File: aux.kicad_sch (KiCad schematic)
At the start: 4 parts

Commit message: Schematic complete, maybe
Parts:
- removed U?: ADuM5211, Package_SO:SSOP-20_5.3x7.2mm_P0.65mm, symbol Isolator:ADuM5211
- added C853: 10u, Capacitor_SMD:C_0603_1608Metric, symbol Device:C
- added D85: BZX84C5V6, Package_TO_SOT_SMD:SOT-23, symbol Parts:BZX84Cxx
- added J85: USB_C_Receptacle_USB2.0_16P, symbol Connector:USB_C_Receptacle_USB2.0_16P
- added J86: Conn_01x02_Pin, symbol Connector:Conn_01x02_Pin
- added L86: 100, Inductor_SMD:L_0603_1608Metric, symbol Parts:L_Ferrite_Power
- added Q81: Si2301CDS, Package_TO_SOT_SMD:SOT-23, symbol External:Si2301CDS
- added Q82: AO3400A, Package_TO_SOT_SMD:SOT-23, symbol Transistor_FET:AO3400A
- added R563, R564: 100k, symbol Device:R
- added R851, R852: 5k1, symbol Device:R
- C851, C852: renamed from C?; LCSC (none) -> C307331
- U85: renamed from U?; footprint RTE0016D -> Package_DFN_QFN:Texas_RTE0016D_WQFN-16-1EP_3x3mm_P0.5mm_EP0.8x0.8mm; LCSC (none) -> C2863226
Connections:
- net GNDPWR: now also C853.2, D85.1 (A), J85.A1 (GND), J85.A12 (GND), J85.B1 (GND), J85.B12 (GND), J85.S1 (SHIELD), Q82.2 (S), R564.1, R851.2, R852.2
- new net: Q81.1 (G), Q82.3 (D), R563.2
- new net: J85.A5 (CC1), R851.1
- new net: J85.B5 (CC2), R852.1
- new net: J85.A4 (VBUS), J85.A9 (VBUS), J85.B4 (VBUS), J85.B9 (VBUS), L86.1
- new net +5V: C853.1, J86.2 (Pin_2), Q81.3 (D)
- new net +5VP: D85.3 (K), J86.1 (Pin_1), L86.2, Q81.2 (S), R563.1
- new net PWR_EN: Q82.1 (G), R564.2
- new net USB_D+: J85.A6 (D+), J85.B6 (D+)
- new net USB_D-: J85.A7 (D-), J85.B7 (D-)
- no-connect marks 1 -> 3
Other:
- moved on the sheet: C851, C852, U85

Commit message: Part selection
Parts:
- J85, J86: now left out of the parts list
- Q81: LCSC (none) -> C10487
- Q82: LCSC (none) -> C20917
- R563, R564: footprint (none) -> Resistor_SMD:R_0402_1005Metric; LCSC (none) -> C25741
- R851, R852: footprint (none) -> Resistor_SMD:R_0402_1005Metric; LCSC (none) -> C25905
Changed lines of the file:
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@@
+			)
+		)
+		(property "LCSC" "C10487"
+			(at 129.54 29.21 90)
+			(effects
+				(font
+					(size 1.27 1.27)
+				)
+				(hide yes)
 			)
 		)
@@
 			)
 		)
-		(property "Footprint" ""
+		(property "Footprint" "Resistor_SMD:R_0402_1005Metric"
 			(at 100.33 33.528 90)
 			(effects
@@
 			)
 		)
+		(property "LCSC" "C25905"
+			(at 100.33 31.75 90)
+			(effects
+				(font
+					(size 1.27 1.27)
+				)
+				(hide yes)
+			)
+		)
 		(pin "1"
 		)
@@
 			)
 		)
-		(property "Footprint" ""
+		(property "Footprint" "Resistor_SMD:R_0402_1005Metric"
 			(at 124.46 34.798 90)
 			(effects
@@
 		(property "Description" "Resistor"
 			(at 124.46 33.02 0)
+			(effects
+				(font
+					(size 1.27 1.27)
+				)
+				(hide yes)
+			)
+		)
+		(property "LCSC" "C25741"
+			(at 124.46 33.02 90)
 			(effects
 				(font
@@
 			)
 		)
-		(property "Footprint" ""
+		(property "Footprint" "Resistor_SMD:R_0402_1005Metric"
 			(at 100.33 32.512 90)
 			(effects
@@
 			)
 		)
+		(property "LCSC" "C25905"
+			(at 100.33 34.29 90)
+			(effects
+				(font
+					(size 1.27 1.27)
+				)
+				(hide yes)
+			)
+		)
 		(pin "1"
 		)
@@
 		(unit 1)
 		(exclude_from_sim no)
-		(in_bom yes)
+		(in_bom no)
 		(on_board yes)
 		(dnp no)
@@
 		(unit 1)
 		(exclude_from_sim no)
-		(in_bom yes)
+		(in_bom no)
 		(on_board yes)
 		(dnp no)
@@
 			)
 		)
+		(property "LCSC" "C20917"
+			(at 132.08 41.91 0)
+			(effects
+				(font
+					(size 1.27 1.27)
+				)
+				(hide yes)
+			)
+		)
 		(pin "1"
 		)
@@
 			)
 		)
-		(property "Footprint" ""
+		(property "Footprint" "Resistor_SMD:R_0402_1005Metric"
 			(at 135.382 45.72 90)
 			(effects
@@
 			(effects
 				(font
+					(size 1.27 1.27)
+				)
+				(hide yes)
+			)
+		)
+		(property "LCSC" "C25741"
+			(at 137.16 45.72 90)
+			(effects
+				(font

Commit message: ERC passes.
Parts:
- added RN81: LT5400-1, Package_SO:MSOP-8-1EP_3x3mm_P0.65mm_EP1.68x1.88mm, symbol Parts:LT5400
- D85: value BZX84C5V6 -> BZX384 5V6; footprint Package_TO_SOT_SMD:SOT-23 -> Diode_SMD:D_SOD-323; symbol Parts:BZX84Cxx -> Parts:BZX384xxxx; LCSC (none) -> C22395563
- renumbered R563 to R853, R564 to R854
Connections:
- net +5VP: now also D85.1 (K); no longer D85.3 (K)
- net GNDPWR: now also D85.2 (A), RN81.1, RN81.2, RN81.3, RN81.4, RN81.5, RN81.6, RN81.7, RN81.8, RN81.9; no longer D85.1 (A)

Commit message: Everything assigned except for wierd shit.
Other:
- moved on the sheet: C851, C852, U85

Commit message: Layout underway
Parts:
- J85: footprint (none) -> Connector_USB:USB_C_Receptacle_GCT_USB4105-xx-A_16P_TopMnt_Horizontal
- J86: footprint (none) -> Parts:PinHeader_1x02_P2.54mm_Vertical
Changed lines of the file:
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@@
 			)
 		)
-		(property "Footprint" ""
+		(property "Footprint" "Parts:PinHeader_1x02_P2.54mm_Vertical"
 			(at 165.1 29.21 0)
 			(effects
@@
 			)
 		)
-		(property "Footprint" ""
+		(property "Footprint" "Connector_USB:USB_C_Receptacle_GCT_USB4105-xx-A_16P_TopMnt_Horizontal"
 			(at 85.09 41.91 0)
 			(effects

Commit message: Whew.  DACs routed
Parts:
- Q81, Q82: footprint Package_TO_SOT_SMD:SOT-23 -> Parts:SOT-23
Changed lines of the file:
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@@
 			)
 		)
-		(property "Footprint" "Package_TO_SOT_SMD:SOT-23"
+		(property "Footprint" "Parts:SOT-23"
 			(at 127.635 24.13 0)
 			(effects
@@
 			)
 		)
-		(property "Footprint" "Package_TO_SOT_SMD:SOT-23"
+		(property "Footprint" "Parts:SOT-23"
 			(at 127 43.815 0)
 			(effects
@@
 			)
 		)
-		(property "Datasheet" "1A working"
+		(property "Datasheet" "2A / 50mOhm"
 			(at 104.14 26.67 0)
 			(effects

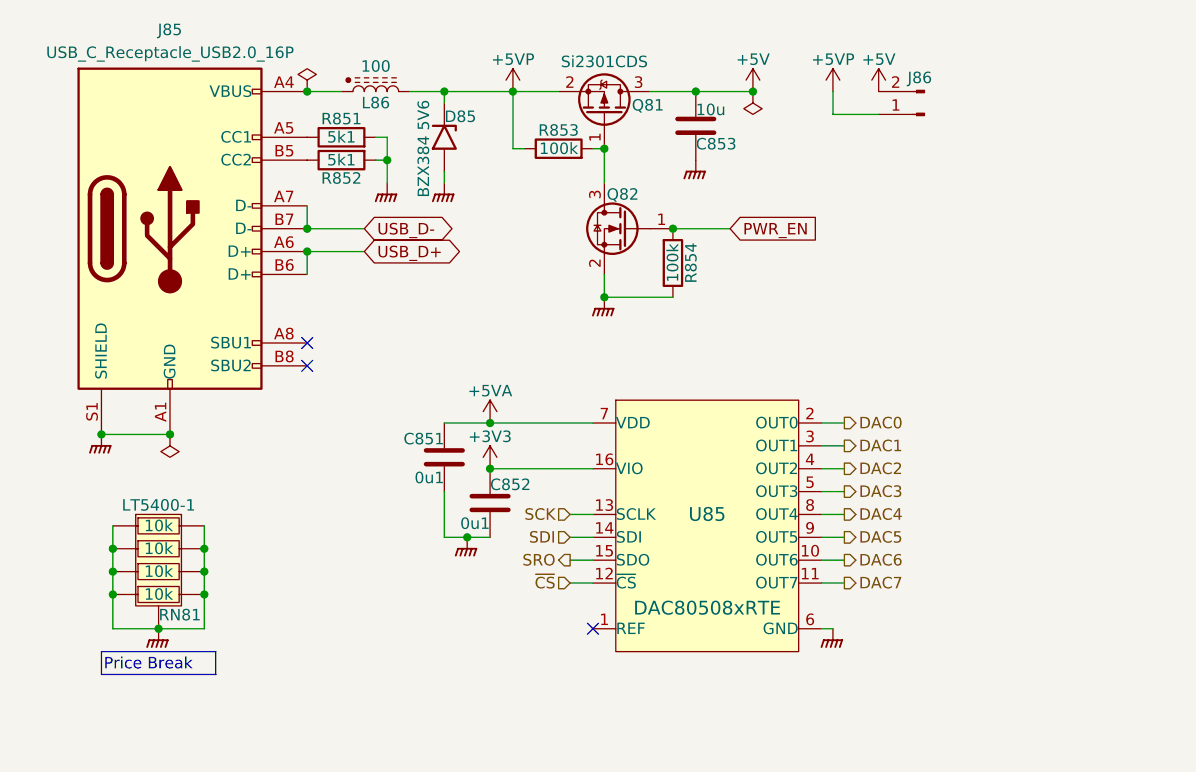
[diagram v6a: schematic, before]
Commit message: Tweaks following spice simulation.
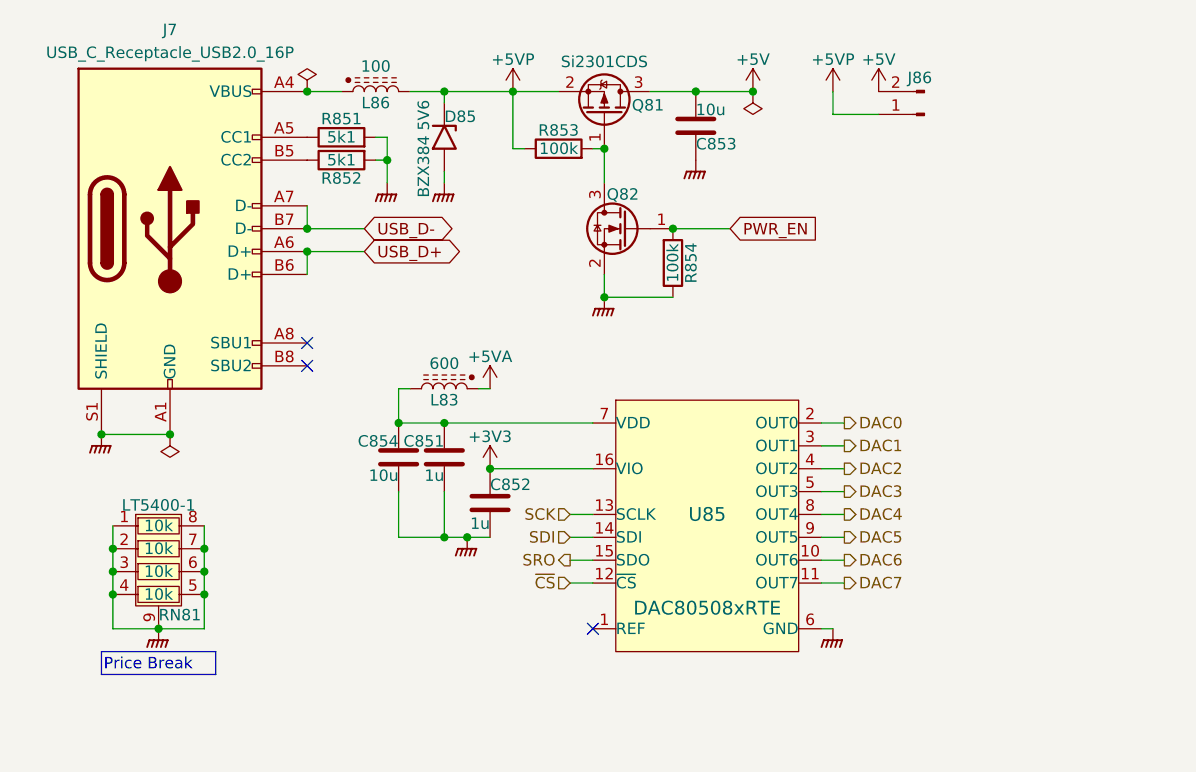
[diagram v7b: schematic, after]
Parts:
- added C854: 10u, Capacitor_SMD:C_0603_1608Metric, symbol Device:C
- added L83: 600, Inductor_SMD:L_0603_1608Metric, symbol Parts:L_Ferrite_Power
- C851, C852: value 0u1 -> 1u; LCSC C307331 -> C52923
- RN81: footprint Package_SO:MSOP-8-1EP_3x3mm_P0.65mm_EP1.68x1.88mm -> Parts:MSOP-8-1EP_3x3mm_P0.65mm_EP1.68x1.88mm
- renumbered J85 to J7
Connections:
- net +5VA: now also L83.1; no longer C851.1, U85.7 (VDD)
- net GNDPWR: now also C854.2
- new net: C851.1, C854.1, L83.2, U85.7 (VDD)
